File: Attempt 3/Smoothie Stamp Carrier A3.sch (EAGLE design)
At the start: 33 parts

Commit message: Motors consolidated, 4 mosfets placed, first glcd attempt
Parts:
- added C44, C45, C46, C47: 10uF, rcl:C-EU050-025X075
- added JP11: (no value), SparkFun-Connectors:M02LOCK
- added JP12, JP13, JP14, JP15: (no value), SparkFun-Connectors:M02PTH
- added JP16: (no value), SparkFun-Connectors:M03LOCK
- added Q1, Q2, Q3, Q4: STP55NF06L, transistor-power:IRF512
- added R10, R11, R12, R9: 4.7k, rcl:R-EU_0207/5V
- added R13, R15, R17, R21, R42: 100k, rcl:R-EU_0204/2V
- added R14, R16, R18, R22, R37: 10r, rcl:R-EU_0204/2V
- added T2: BC817, SparkFun-DiscreteSemi:TRANSISTOR_NPN2N3904
- added X1: 5566-24, con-molex:5566-24
- added X2, X3, X4, X5, X6, X8: MSTBA2, con-phoenix-508:MSTBA2
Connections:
- net N$50 renamed P1_22-3RD-SMALL-FET
- net N$51 renamed P1_23-3RD-LARGE-FET
- new net +5V: X1-21.S
- new net +5VSB: X1-9.S
- new net 12V: C1.+, C2.+, C3.+, C31.+, C4.+, U$2.VMOT, U$3.VMOT, U$4.VMOT, U$5.VMOT, U$6.VMOT, X1-10.S, X1-11.S, X8-1.1
- new net 12V1: X2-1.1, X3-1.1, X4-1.1, X5-1.1, X6-1.1
- new net AGND: C44.2, C45.2, C46.2, C47.2, JP12.1, JP13.1, JP14.1, JP15.1, U$1.AGND
- new net AVCC: R10.2, R11.2, R12.2, R9.2, U$1.AVCC
- new net N$50: Q3.D, X5-2.1
- new net N$51: Q4.G, R22.2
- new net N$52: U$1.X_MIN
- new net N$53: U$1.X_MAX
- new net N$54: U$1.Y_MIN
- new net N$55: U$1.Y_MAX
- new net N$56: U$1.Z_MIN
- new net N$57: U$1.Z_MAX
- new net N$58: Q4.D, X6-2.1
- new net N$59: Q1.G, R14.2
- new net N$60: JP16.2, T2.C
- new net N$61: R37.2, R42.2, T2.B
- new net N$64: U$1.RX_0
- new net N$65: U$1.TX_0
- new net P2.6_FAN_FET: R15.1, R16.1, R37.1, U$1.P2.6_FAN_FET
- new net P2.7_HOTEND_FET: R13.1, R14.1, U$1.P2.7_HOTEND_FET
- new net PSUON: JP11.2, X1-16.S
- new net PWM0_PSU_OUT: R21.1, R22.1, U$1.PWM0_PSU_OUT
- new net PWM1_BED_HEATER: R17.1, R18.1, U$1.PWM1_BED_HEATER
- new net TH1_HOTEND: C45.1, JP13.2, R10.1, U$1.TH1_HOTEND
- new net TH2_BED: C44.1, JP12.2, R9.1, U$1.TH2_BED
- new net TH3: C46.1, JP14.2, R11.1, U$1.TH3
- new net TH4: C47.1, JP15.2, R12.1, U$1.TH4
- net 24V: now also JP16.1; no longer C1.+, C2.+, C3.+, C31.+, C4.+, U$2.VMOT, U$3.VMOT, U$4.VMOT, U$5.VMOT, U$6.VMOT
- net 5V: now also JP16.3
- net GND: now also JP11.1, Q1.S, Q2.S, Q3.S, Q4.S, R13.2, R15.2, R17.2, R21.2, R42.1, T2.E, X1-17.S, X1-18.S, X1-19.S, X2-2.1, X8-2.1
- net N$46: now also Q1.D, X3-2.1; no longer U$1.P2.7_HOTEND_FET
- net N$47: now also Q2.G, R16.2; no longer U$1.PWM1_BED_HEATER
- net N$48: now also Q2.D, X4-2.1; no longer U$1.P2.6_FAN_FET
- net N$49: now also Q3.G, R18.2; no longer U$1.PWM0_PSU_OUT
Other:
- note added: "(PS-ON)"

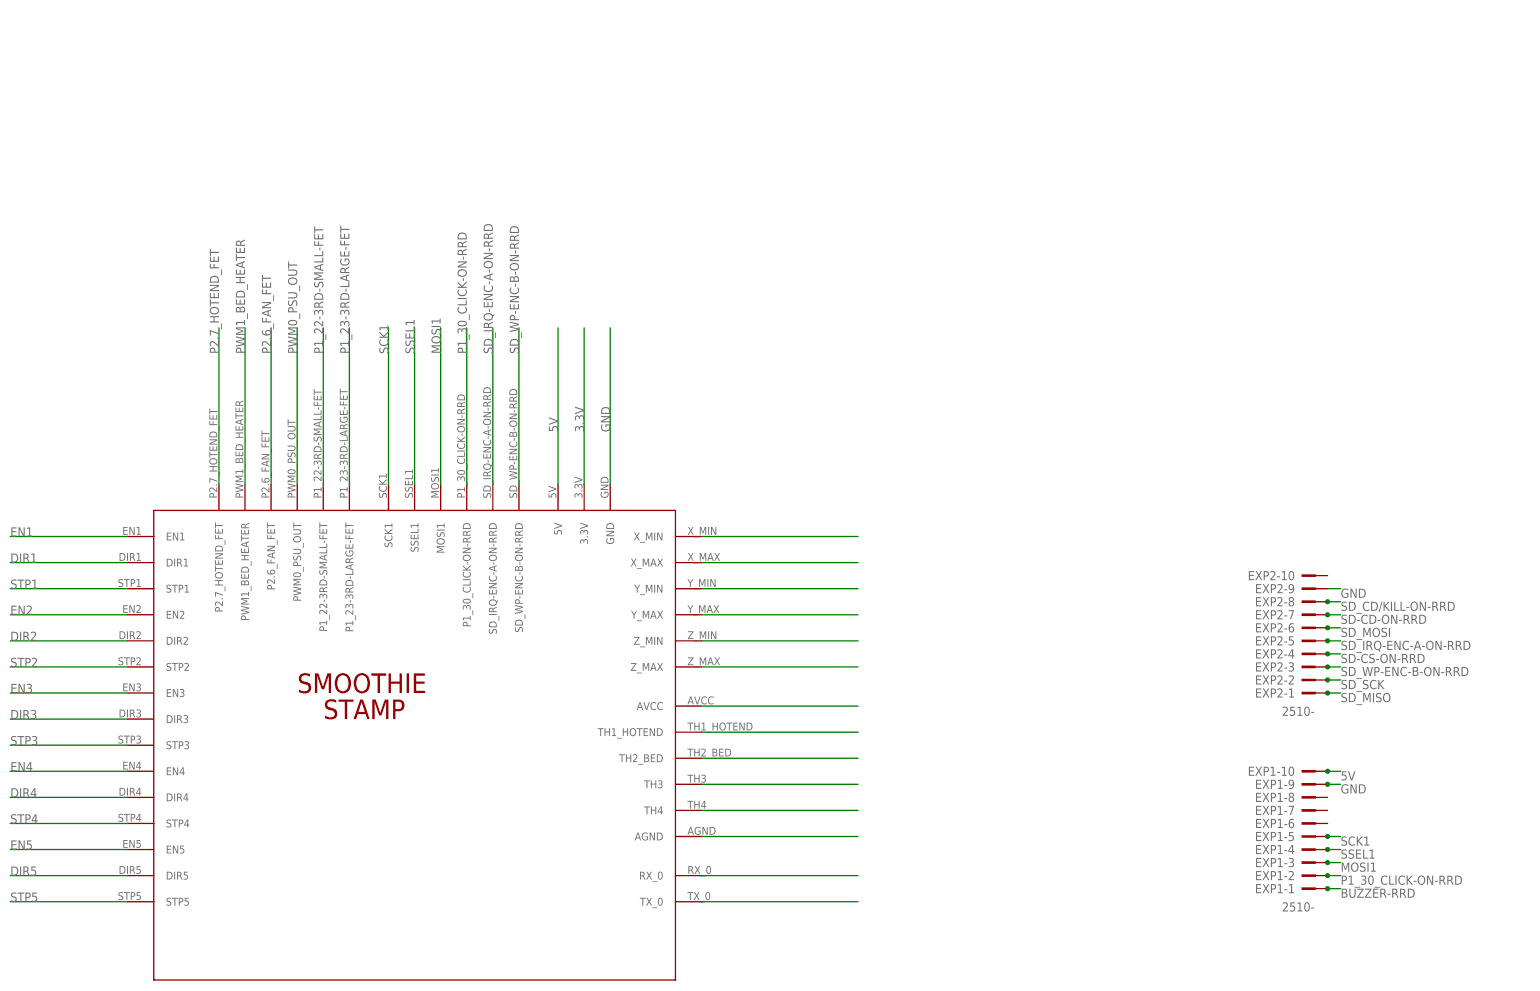
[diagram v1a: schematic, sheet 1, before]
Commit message: Dedicated Power In for Bed MOSFET, rev1 board don
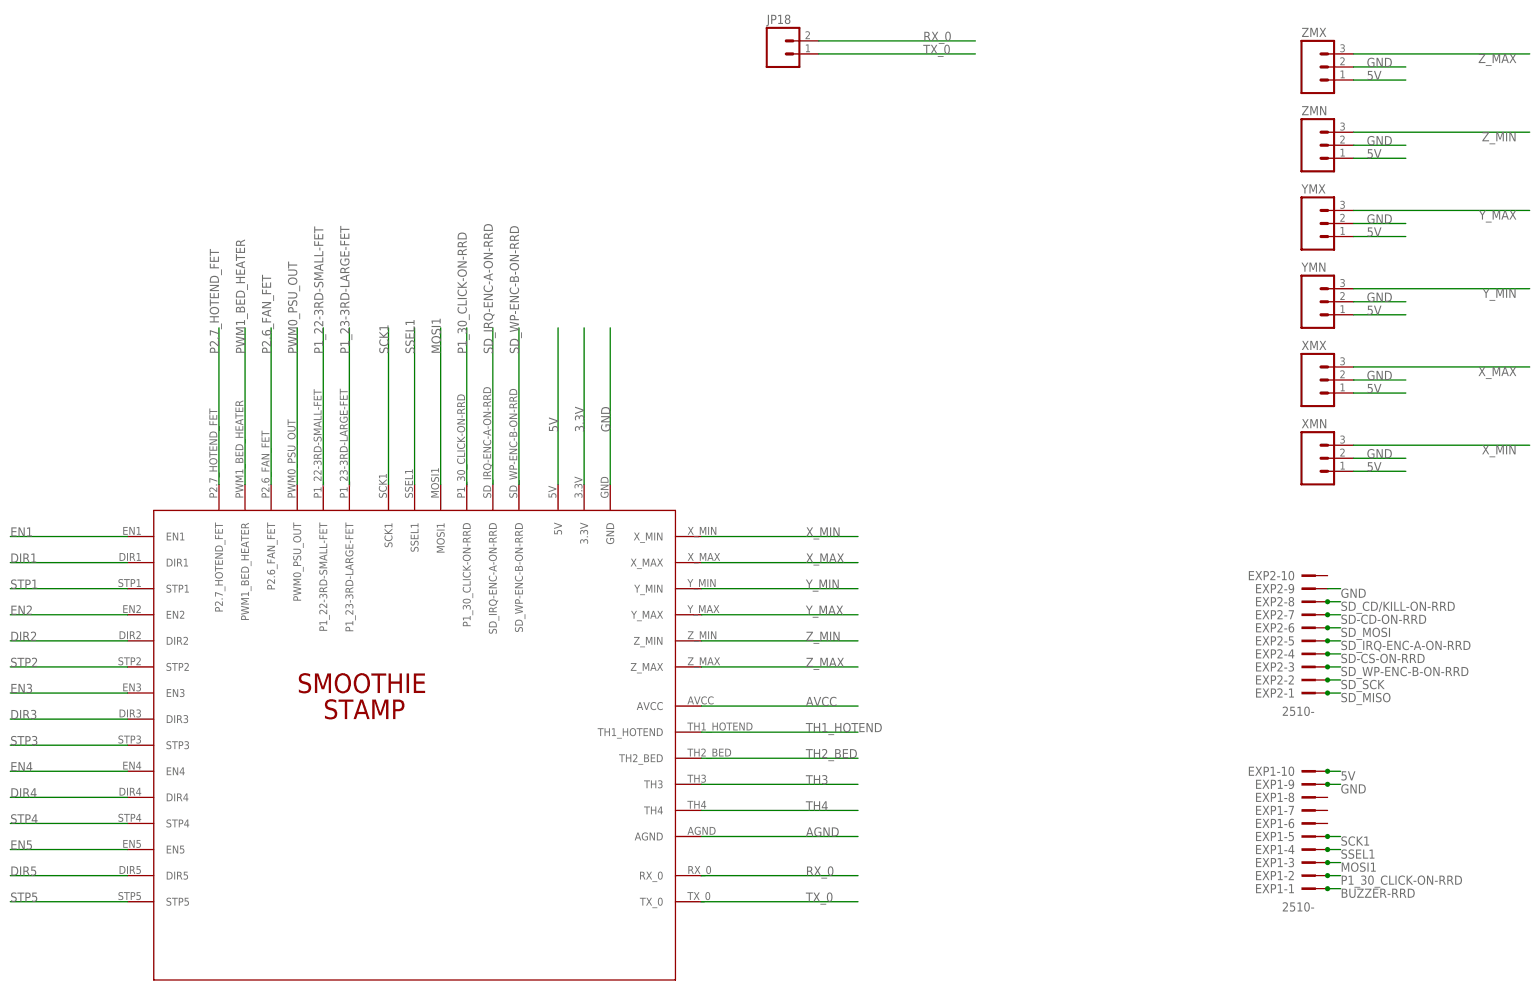
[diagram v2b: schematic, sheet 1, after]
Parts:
- added JP17, JP18: (no value), SparkFun-Connectors:M02LOCK
- added R23: 10r, rcl:R-EU_0204/2V
- added R24: 100k, rcl:R-EU_0204/2V
- added T1: BC817, SparkFun-DiscreteSemi:TRANSISTOR_NPN2N3904
- added X7: MSTBA2, con-phoenix-508:MSTBA2
- added XMN, XMX, YMN, YMX, ZMN, ZMX: (no value), SparkFun-Connectors:M03LOCK
- JP16: device SparkFun-Connectors:M03LOCK -> SparkFun-Connectors:M02LOCK
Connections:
- removed net 24V: JP16.1
- removed net N$52: U$1.X_MIN
- removed net N$53: U$1.X_MAX
- removed net N$54: U$1.Y_MIN
- removed net N$55: U$1.Y_MAX
- removed net N$56: U$1.Z_MIN
- removed net N$57: U$1.Z_MAX
- removed net N$64: U$1.RX_0
- removed net N$65: U$1.TX_0
- new net 12V2: X5-1.1, X7-1.1
- new net N$62: JP17.2, T1.C
- new net N$63: R23.2, R24.2, T1.B
- new net RX_0: JP18.2, U$1.RX_0
- new net TX_0: JP18.1, U$1.TX_0
- new net X_MAX: U$1.X_MAX, XMX.3
- new net X_MIN: U$1.X_MIN, XMN.3
- new net Y_MAX: U$1.Y_MAX, YMX.3
- new net Y_MIN: U$1.Y_MIN, YMN.3
- new net Z_MAX: U$1.Z_MAX, ZMX.3
- new net Z_MIN: U$1.Z_MIN, ZMN.3
- net 12V: now also JP16.1, JP17.1
- net 12V1: no longer X5-1.1
- net 5V: now also XMN.1, XMX.1, YMN.1, YMX.1, ZMN.1, ZMX.1; no longer JP16.3
- net GND: now also R24.1, T1.E, X7-2.1, XMN.2, XMX.2, YMN.2, YMX.2, ZMN.2, ZMX.2
- net P1_22-3RD-SMALL-FET: now also R23.1
- net P1_23-3RD-LARGE-FET: now also R37.1
- net P2.6_FAN_FET: no longer R37.1
